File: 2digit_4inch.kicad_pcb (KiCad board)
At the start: 2 copper layers, 180.7 x 138.3 mm, 29 parts, among them P1 CONN_20X2, P2 CONN_2, P3 CONN_20X2, P4 CONN_2, P5 CONN_16X2, P6 CONN_2, P7 CONN_2, Q1 TIP127, Q2 TIP127, U1 ULN2003A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

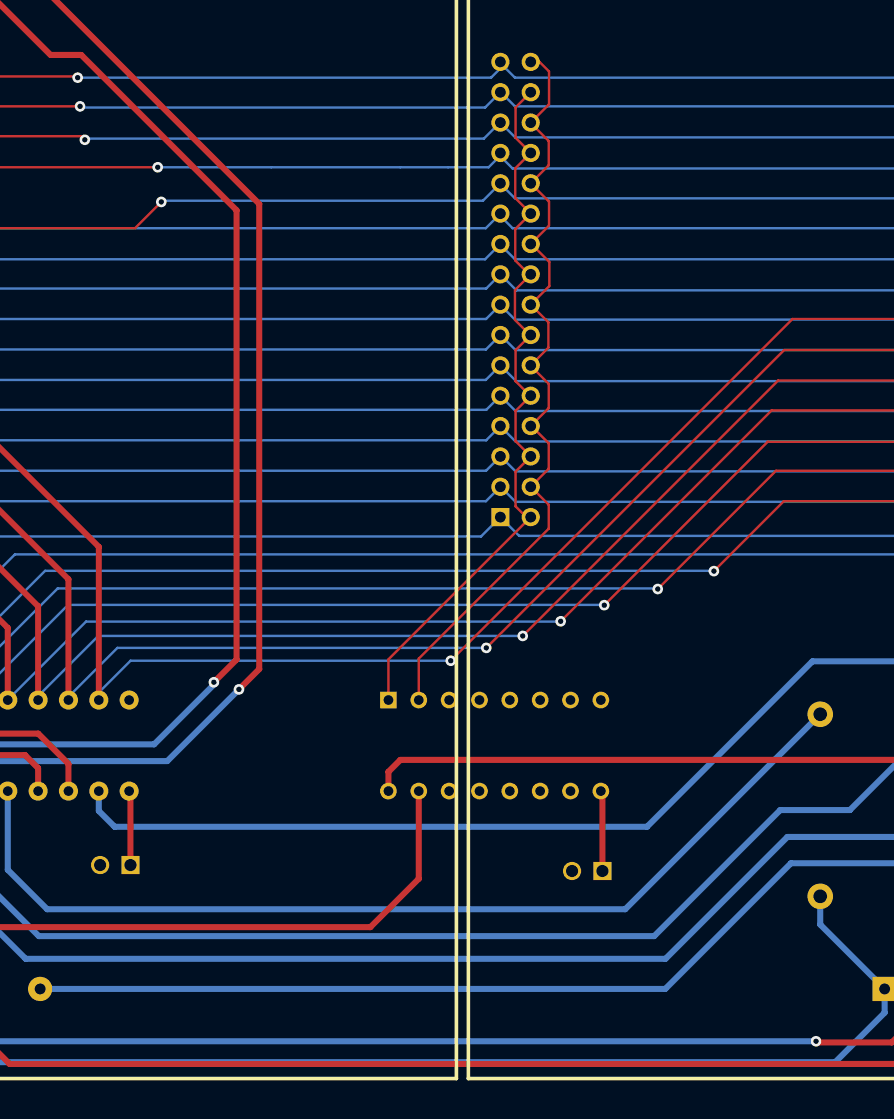
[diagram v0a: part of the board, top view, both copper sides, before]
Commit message: Via dimension updated
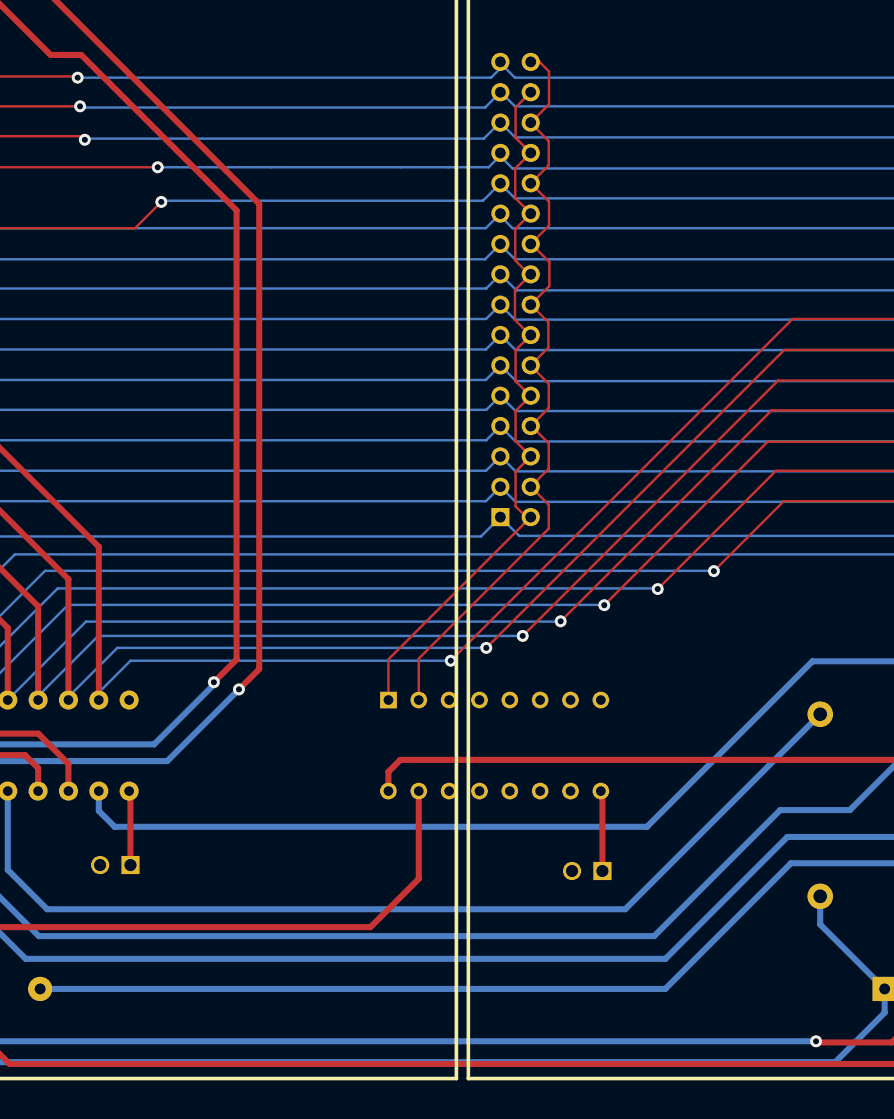
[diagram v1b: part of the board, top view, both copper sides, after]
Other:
- net class DIGIT_SELECT: via_dia 0.889 -> 1
- net class Default: via_dia 0.889 -> 1
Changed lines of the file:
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@@
     (links 112)
     (no_connects 0)
-    (area 54.765717 21.64 248.9104 222.643)
+    (area 54.765717 78.919996 248.9104 222.643)
     (thickness 1.6)
     (drawings 30)
@@
     (segment_width 0.2)
     (edge_width 0.1)
-    (via_size 0.889)
+    (via_size 1)
     (via_drill 0.635)
     (via_min_size 0.889)
@@
     (visible_elements 7FFFDFFF)
     (pcbplotparams
-      (layerselection 23101441)
+      (layerselection 292323329)
       (usegerberextensions true)
       (excludeedgelayer true)
@@
       (drillshape 0)
       (scaleselection 1)
-      (outputdirectory ""))
+      (outputdirectory 2d_4inch_gerbers/))
   )
   (net 0 "")
@@
     (clearance 0.254)
     (trace_width 0.508)
-    (via_dia 0.889)
+    (via_dia 1)
     (via_drill 0.635)
     (uvia_dia 0.508)
@@
     (clearance 0.254)
     (trace_width 0.2032)
-    (via_dia 0.889)
+    (via_dia 1)
     (via_drill 0.635)
     (uvia_dia 0.508)
@@
   (segment (start 184.7 166.05) (end 240 166.05) (width 0.2032) (layer F.Cu) (net 2))
   (segment (start 178.85 171.9) (end 184.7 166.05) (width 0.2032) (layer F.Cu) (net 2))
-  (via (at 178.85 171.9) (size 0.889) (layers F.Cu B.Cu) (net 2))
+  (via (at 178.85 171.9) (size 1) (layers F.Cu B.Cu) (net 2))
   (segment (start 178.825 171.875) (end 178.85 171.9) (width 0.2032) (layer B.Cu) (net 2))
   (segment (start 122.875 171.875) (end 178.825 171.875) (width 0.2032) (layer B.Cu) (net 2))
@@
   (segment (start 184.05 163.5) (end 240.01 163.5) (width 0.2032) (layer F.Cu) (net 3))
   (segment (start 174.15 173.4) (end 184.05 163.5) (width 0.2032) (layer F.Cu) (net 3))
-  (via (at 174.15 173.4) (size 0.889) (layers F.Cu B.Cu) (net 3))
+  (via (at 174.15 173.4) (size 1) (layers F.Cu B.Cu) (net 3))
   (segment (start 174.1 173.35) (end 174.15 173.4) (width 0.2032) (layer B.Cu) (net 3))
   (segment (start 123.925 173.35) (end 174.1 173.35) (width 0.2032) (layer B.Cu) (net 3))
@@
   (segment (start 183.35 161.075) (end 239.895 161.075) (width 0.2032) (layer F.Cu) (net 4))
   (segment (start 169.675 174.75) (end 183.35 161.075) (width 0.2032) (layer F.Cu) (net 4))
-  (via (at 169.675 174.75) (size 0.889) (layers F.Cu B.Cu) (net 4))
+  (via (at 169.675 174.75) (size 1) (layers F.Cu B.Cu) (net 4))
   (segment (start 169.65 174.725) (end 169.675 174.75) (width 0.2032) (layer B.Cu) (net 4))
   (segment (start 124.8 174.725) (end 169.65 174.725) (width 0.2032) (layer B.Cu) (net 4))
@@
   (segment (start 132.7 140.9) (end 159.52 140.9) (width 0.2032) (layer B.Cu) (net 8))
   (segment (start 132.6 141) (end 132.7 140.9) (width 0.2032) (layer B.Cu) (net 8))
-  (via (at 132.6 141) (size 0.889) (layers F.Cu B.Cu) (net 8))
+  (via (at 132.6 141) (size 1) (layers F.Cu B.Cu) (net 8))
   (segment (start 130.4 143.2) (end 132.6 141) (width 0.2032) (layer F.Cu) (net 8))
   (segment (start 75.6 143.2) (end 130.4 143.2) (width 0.2032) (layer F.Cu) (net 8))
@@
   (segment (start 73.73 137.23) (end 74.6 138.1) (width 0.2032) (layer F.Cu) (net 9))
   (segment (start 74.6 138.1) (end 132.3 138.1) (width 0.2032) (layer F.Cu) (net 9))
-  (via (at 132.3 138.1) (size 0.889) (layers F.Cu B.Cu) (net 9))
+  (via (at 132.3 138.1) (size 1) (layers F.Cu B.Cu) (net 9))
   (segment (start 132.3 138.1) (end 141.8 138.1) (width 0.2032) (layer B.Cu) (net 9))
   (segment (start 141.8 138.1) (end 152.6 138.1) (width 0.2032) (layer B.Cu) (net 9))
@@
   (segment (start 125.9 135.5) (end 74.93 135.5) (width 0.2032) (layer F.Cu) (net 10))
   (segment (start 126.2 135.8) (end 125.9 135.5) (width 0.2032) (layer F.Cu) (net 10))
-  (via (at 126.2 135.8) (size 0.889) (layers F.Cu B.Cu) (net 10))
+  (via (at 126.2 135.8) (size 1) (layers F.Cu B.Cu) (net 10))
   (segment (start 126.3 135.7) (end 126.2 135.8) (width 0.2032) (layer B.Cu) (net 10))
   (segment (start 159.6 135.7) (end 126.3 135.7) (width 0.2032) (layer B.Cu) (net 10))
@@
   (segment (start 125.9 133.1) (end 159.7 133.1) (width 0.2032) (layer B.Cu) (net 11))
   (segment (start 125.8 133) (end 125.9 133.1) (width 0.2032) (layer B.Cu) (net 11))
-  (via (at 125.8 133) (size 0.889) (layers F.Cu B.Cu) (net 11))
+  (via (at 125.8 133) (size 1) (layers F.Cu B.Cu) (net 11))
   (segment (start 74.9 133) (end 125.8 133) (width 0.2032) (layer F.Cu) (net 11))
   (segment (start 73.73 131.83) (end 74.9 133) (width 0.2032) (layer F.Cu) (net 11))
@@
   (segment (start 125.5 130.5) (end 75.01 130.5) (width 0.2032) (layer F.Cu) (net 12))
   (segment (start 125.6 130.6) (end 125.5 130.5) (width 0.2032) (layer F.Cu) (net 12))
-  (via (at 125.6 130.6) (size 0.889) (layers F.Cu B.Cu) (net 12))
+  (via (at 125.6 130.6) (size 1) (layers F.Cu B.Cu) (net 12))
   (segment (start 160.2 130.6) (end 125.6 130.6) (width 0.2032) (layer B.Cu) (net 12))
   (segment (start 160.98 129.82) (end 160.2 130.6) (width 0.2032) (layer B.Cu) (net 12))
@@
   (segment (start 183.675 158.45) (end 239.98 158.45) (width 0.2032) (layer F.Cu) (net 23))
   (segment (start 166.025 176.1) (end 183.675 158.45) (width 0.2032) (layer F.Cu) (net 23))
-  (via (at 166.025 176.1) (size 0.889) (layers F.Cu B.Cu) (net 23))
+  (via (at 166.025 176.1) (size 1) (layers F.Cu B.Cu) (net 23))
   (segment (start 166 176.125) (end 166.025 176.1) (width 0.2032) (layer B.Cu) (net 23))
   (segment (start 126.3 176.125) (end 166 176.125) (width 0.2032) (layer B.Cu) (net 23))
@@
   (segment (start 184.225 155.95) (end 239.94 155.95) (width 0.2032) (layer F.Cu) (net 24))
   (segment (start 162.85 177.325) (end 184.225 155.95) (width 0.2032) (layer F.Cu) (net 24))
-  (via (at 162.85 177.325) (size 0.889) (layers F.Cu B.Cu) (net 24))
+  (via (at 162.85 177.325) (size 1) (layers F.Cu B.Cu) (net 24))
   (segment (start 127.325 177.325) (end 162.85 177.325) (width 0.2032) (layer B.Cu) (net 24))
   (segment (start 122.29 182.36) (end 127.325 177.325) (width 0.2032) (layer B.Cu) (net 24))
@@
   (segment (start 184.725 153.4) (end 239.95 153.4) (width 0.2032) (layer F.Cu) (net 25))
   (segment (start 159.8 178.325) (end 184.725 153.4) (width 0.2032) (layer F.Cu) (net 25))
-  (via (at 159.8 178.325) (size 0.889) (layers F.Cu B.Cu) (net 25))
+  (via (at 159.8 178.325) (size 1) (layers F.Cu B.Cu) (net 25))
   (segment (start 128.925 178.325) (end 159.8 178.325) (width 0.2032) (layer B.Cu) (net 25))
   (segment (start 124.83 182.42) (end 128.925 178.325) (width 0.2032) (layer B.Cu) (net 25))
@@
   (segment (start 185.425 150.8) (end 240.01 150.8) (width 0.2032) (layer F.Cu) (net 26))
   (segment (start 156.825 179.4) (end 185.425 150.8) (width 0.2032) (layer F.Cu) (net 26))
-  (via (at 156.825 179.4) (size 0.889) (layers F.Cu B.Cu) (net 26))
+  (via (at 156.825 179.4) (size 1) (layers F.Cu B.Cu) (net 26))
   (segment (start 130.025 179.4) (end 156.825 179.4) (width 0.2032) (layer B.Cu) (net 26))
   (segment (start 127.37 182.055) (end 130.025 179.4) (width 0.2032) (layer B.Cu) (net 26))
@@
   (segment (start 187.5 211.35) (end 193.74 211.35) (width 0.508) (layer F.Cu) (net 30))
   (segment (start 187.4 211.25) (end 187.5 211.35) (width 0.508) (layer F.Cu) (net 30))
-  (via (at 187.4 211.25) (size 0.889) (layers F.Cu B.Cu) (net 30))
+  (via (at 187.4 211.25) (size 1) (layers F.Cu B.Cu) (net 30))
   (segment (start 108.6 211.25) (end 187.4 211.25) (width 0.508) (layer B.Cu) (net 30))
   (segment (start 107.22 209.87) (end 108.6 211.25) (width 0.508) (layer B.Cu) (net 30))
@@
   (segment (start 138.9 179.3) (end 138.9 141.7) (width 0.508) (layer F.Cu) (net 48))
   (segment (start 137 181.2) (end 138.9 179.3) (width 0.508) (layer F.Cu) (net 48))
-  (via (at 137 181.2) (size 0.889) (layers F.Cu B.Cu) (net 48))
+  (via (at 137 181.2) (size 1) (layers F.Cu B.Cu) (net 48))
   (segment (start 137 181.4) (end 137 181.2) (width 0.508) (layer B.Cu) (net 48))
   (segment (start 132 186.4) (end 137 181.4) (width 0.508) (layer B.Cu) (net 48))
@@
   (segment (start 140.8 180.1) (end 140.8 141.17) (width 0.508) (layer F.Cu) (net 49))
   (segment (start 139.1 181.8) (end 140.8 180.1) (width 0.508) (layer F.Cu) (net 49))
-  (via (at 139.1 181.8) (size 0.889) (layers F.Cu B.Cu) (net 49))
+  (via (at 139.1 181.8) (size 1) (layers F.Cu B.Cu) (net 49))
   (segment (start 133.1 187.8) (end 139.1 181.8) (width 0.508) (layer B.Cu) (net 49))
   (segment (start 113.4 187.8) (end 133.1 187.8) (width 0.508) (layer B.Cu) (net 49))
